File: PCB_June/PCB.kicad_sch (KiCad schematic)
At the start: 26 parts, among them J2 FH34SRJ-24S-0.5SH_99_, J9 61302421121, Q1 BSS138, Q2 S8050, U3 AO3401

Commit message: yur
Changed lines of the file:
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@@
 	(wire
 		(pts
-			(xy 53.34 130.81) (xy 60.96 130.81)
+			(xy 53.34 130.81) (xy 73.66 130.81)
 		)
 		(stroke
@@
 	(wire
 		(pts
-			(xy 53.34 128.27) (xy 60.96 128.27)
+			(xy 53.34 128.27) (xy 73.66 128.27)
 		)
 		(stroke
@@
 	(wire
 		(pts
-			(xy 53.34 123.19) (xy 60.96 123.19)
+			(xy 53.34 123.19) (xy 73.66 123.19)
 		)
 		(stroke
@@
 	(wire
 		(pts
-			(xy 53.34 125.73) (xy 60.96 125.73)
+			(xy 53.34 125.73) (xy 73.66 125.73)
 		)
 		(stroke
@@
 			)
 			(justify left bottom)
+		)
+	)
+	(global_label "EPD_CS"
+		(shape input)
+		(at 73.66 130.81 0)
+		(fields_autoplaced yes)
+		(effects
+			(font
+				(size 1.27 1.27)
+			)
+			(justify left)
+		)
+		(property "Intersheetrefs" "${INTERSHEET_REFS}"
+			(at 83.7813 130.81 0)
+			(effects
+				(font
+					(size 1.27 1.27)
+				)
+				(justify left)
+				(hide yes)
+			)
+		)
+	)
+	(global_label "EPD_BUSY"
+		(shape input)
+		(at 73.66 123.19 0)
+		(fields_autoplaced yes)
+		(effects
+			(font
+				(size 1.27 1.27)
+			)
+			(justify left)
+		)
+		(property "Intersheetrefs" "${INTERSHEET_REFS}"
+			(at 86.2004 123.19 0)
+			(effects
+				(font
+					(size 1.27 1.27)
+				)
+				(justify left)
+				(hide yes)
+			)
 		)
 	)
@@
 			(effects
 				(font
+					(size 1.27 1.27)
+				)
+				(justify left)
+				(hide yes)
+			)
+		)
+	)
+	(global_label "EPD_RST"
+		(shape input)
+		(at 73.66 125.73 0)
+		(fields_autoplaced yes)
+		(effects
+			(font
+				(size 1.27 1.27)
+			)
+			(justify left)
+		)
+		(property "Intersheetrefs" "${INTERSHEET_REFS}"
+			(at 84.7489 125.73 0)
+			(effects
+				(font
+					(size 1.27 1.27)
+				)
+				(justify left)
+				(hide yes)
+			)
+		)
+	)
+	(global_label "EPD_DC"
+		(shape input)
+		(at 73.66 128.27 0)
+		(fields_autoplaced yes)
+		(effects
+			(font
+				(size 1.27 1.27)
+			)
+			(justify left)
+		)
+		(property "Intersheetrefs" "${INTERSHEET_REFS}"
+			(at 83.8418 128.27 0)
+			(effects
+				(font

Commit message: MCB
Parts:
- C17: value 104 -> 0.1u
- L1: value 10u -> 10uH
- R2, R4: value 10K -> 10k
- R3, R5: value 47K -> 47k
- R6: value 100K -> 100k
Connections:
- net EPD_PWR: now also R3.2, R4.2
- no-connect marks 0 -> 11
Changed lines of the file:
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@@
 		(color 0 0 0 0)
 	)
+	(no_connect
+		(at 53.34 110.49)
+	)
+	(no_connect
+		(at 142.24 119.38)
+	)
+	(no_connect
+		(at 142.24 111.76)
+	)
+	(no_connect
+		(at 119.38 114.3)
+	)
+	(no_connect
+		(at 53.34 148.59)
+	)
+	(no_connect
+		(at 53.34 102.87)
+	)
+	(no_connect
+		(at 142.24 134.62)
+	)
+	(no_connect
+		(at 53.34 118.11)
+	)
+	(no_connect
+		(at 53.34 115.57)
+	)
+	(no_connect
+		(at 119.38 129.54)
+	)
+	(no_connect
+		(at 119.38 116.84)
+	)
 	(wire
 		(pts
@@
 	(wire
 		(pts
-			(xy 91.44 48.26) (xy 96.52 48.26)
-		)
-		(stroke
-			(width 0)
-			(type default)
-		)
-	)
-	(wire
-		(pts
 			(xy 107.95 26.67) (xy 107.95 29.21)
 		)
@@
 	(wire
 		(pts
+			(xy 86.36 48.26) (xy 96.52 48.26)
+		)
+		(stroke
+			(width 0)
+			(type default)
+		)
+	)
+	(wire
+		(pts
 			(xy 114.3 26.67) (xy 107.95 26.67)
 		)
@@
 		)
 	)
-	(label "GND"
-		(at 127 60.96 0)
+	(label "3V3_OUT"
+		(at 36.83 41.91 270)
 		(effects
 			(font
 				(size 1.27 1.27)
 			)
-			(justify left bottom)
+			(justify right bottom)
 		)
 	)
-	(label "RESE"
-		(at 149.86 114.3 0)
+	(label "GND"
+		(at 127 60.96 0)
 		(effects
 			(font
@@
 	)
 	(label "RESE"
-		(at 46.99 22.86 0)
-		(effects
-			(font
-				(size 1.27 1.27)
-			)
-			(justify left bottom)
-		)
-	)
-	(label "3V3_OUT"
-		(at 36.83 46.99 90)
+		(at 149.86 114.3 0)
 		(effects
 			(font
@@
 		)
 	)
-	(label "EPD_PWR"
-		(at 86.36 48.26 0)
+	(label "RESE"
+		(at 46.99 22.86 0)
 		(effects
 			(font
@@
 		)
 	)
-	(label "3V3_OUT"
-		(at 36.83 46.99 90)
-		(effects
-			(font
-				(size 1.27 1.27)
-			)
-			(justify left bottom)
-		)
-	)
 	(label "SUB20"
 		(at 60.96 151.13 0)
@@
 		)
 	)
-	(label "3V3_OUT"
-		(at 36.83 46.99 90)
-		(effects
-			(font
-				(size 1.27 1.27)
-			)
-			(justify left bottom)
-		)
-	)
 	(label "EPD_SCK"
 		(at 149.86 127 0)
@@
 		)
 	)
-	(label "EPD_PWR"
-		(at 86.36 48.26 0)
-		(effects
-			(font
-				(size 1.27 1.27)
-			)
-			(justify left bottom)
-		)
-	)
 	(label "GND"
 		(at 149.86 132.08 0)
@@
 		)
 	)
-	(label "EPD_PWR"
-		(at 86.36 48.26 0)
-		(effects
-			(font
-				(size 1.27 1.27)
-			)
-			(justify left bottom)
-		)
-	)
 	(label "VGL"
 		(at 149.86 139.7 0)
@@
 		)
 	)
-	(label "VGL"
-		(at 60.96 158.75 0)
+	(label "EPD_PWR"
+		(at 86.36 48.26 0)
 		(effects
 			(font
@@
 		)
 	)
-	(label "GND"
-		(at 86.36 43.18 90)
+	(label "VGL"
+		(at 60.96 158.75 0)
 		(effects
 			(font
@@
 		)
 	)
-	(label "EPD_SCK"
-		(at 60.96 133.35 0)
+	(label "GND"
+		(at 86.36 43.18 90)
 		(effects
 			(font
@@
 		)
 	)
-	(label "3V3_OUT"
-		(at 36.83 46.99 90)
+	(label "EPD_SCK"
+		(at 60.96 133.35 0)
 		(effects
 			(font
@@
 		)
 	)
-	(label "EPD_BUSY"
-		(at 149.86 121.92 0)
+	(label "3V3_OUT"
+		(at 130.81 20.32 0)
 		(effects
 			(font
@@
 		)
 	)
-	(label "3V3_OUT"
-		(at 130.81 26.67 0)
+	(label "EPD_BUSY"
+		(at 149.86 121.92 0)
 		(effects
 			(font
@@
 		)
 	)
-	(label "EPD_PWR"
-		(at 86.36 48.26 0)
-		(effects
-			(font
-				(size 1.27 1.27)
-			)
-			(justify left bottom)
-		)
-	)
 	(label "VGH"
 		(at 149.86 137.16 0)
@@
 			)
 		)
-		(property "Value" "47K"
+		(property "Value" "47k"
 			(at 110.49 34.2899 0)
 			(effects
@@
 			)
 		)
-		(property "Value" "10K"
+		(property "Value" "10k"
 			(at 104.14 52.07 90)
 			(effects
@@
 			)
 		)
-		(property "Value" "47K"
+		(property "Value" "47k"
 			(at 99.06 40.6399 0)
 			(effects
@@
 			)
 		)
-		(property "Value" "100K"
+		(property "Value" "100k"
 			(at 113.03 57.1499 0)
 			(effects
@@
 			)
 		)
-		(property "Value" "104"
+		(property "Value" "0.1u"
 			(at 90.17 35.5599 0)
 			(effects
@@
 			)
 		)
-		(property "Value" "10K"
+		(property "Value" "10k"
 			(at 29.21 29.21 90)
 			(effects
@@
 			)
 		)
-		(property "Value" "10u"
+		(property "Value" "10uH"
 			(at 43.18 48.26 90)
 			(effects

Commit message: claire can i get inductor footprint haha
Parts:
- removed L1: 10uH, Inductor_SMD:L_0805_2012Metric_Pad1.05x1.20mm_HandSolder, symbol Device:L
- added L1: WE-MXGI_5030, WE-MXGI_5030:WE-MXGI_5030, symbol WE-MXGI_5030:WE-MXGI_5030
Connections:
- net 3V3_OUT: now also L1.1
- net at C8.2, D3.2 (A), Q1.3 (D): now also L1.2
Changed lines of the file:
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@@
 	)
 	(junction
-		(at 110.49 48.26)
+		(at 34.29 50.8)
 		(diameter 0)
 		(color 0 0 0 0)
 	)
 	(junction
-		(at 121.92 60.96)
+		(at 110.49 48.26)
 		(diameter 0)
 		(color 0 0 0 0)
 	)
 	(junction
-		(at 22.86 161.29)
+		(at 52.07 50.8)
 		(diameter 0)
 		(color 0 0 0 0)
 	)
 	(junction
-		(at 96.52 153.67)
+		(at 121.92 60.96)
 		(diameter 0)
 		(color 0 0 0 0)
 	)
 	(junction
-		(at 52.07 50.8)
+		(at 22.86 161.29)
 		(diameter 0)
 		(color 0 0 0 0)
 	)
 	(junction
-		(at 121.92 40.64)
+		(at 96.52 153.67)
 		(diameter 0)
 		(color 0 0 0 0)
 	)
 	(junction
-		(at 36.83 50.8)
+		(at 121.92 40.64)
 		(diameter 0)
 		(color 0 0 0 0)
@@
 	(wire
 		(pts
-			(xy 21.59 50.8) (xy 21.59 64.77)
+			(xy 52.07 50.8) (xy 52.07 64.77)
 		)
 		(stroke
@@
 	(wire
 		(pts
-			(xy 53.34 151.13) (xy 71.12 151.13)
+			(xy 21.59 50.8) (xy 21.59 64.77)
 		)
 		(stroke
@@
 	(wire
 		(pts
-			(xy 53.34 130.81) (xy 73.66 130.81)
+			(xy 53.34 151.13) (xy 71.12 151.13)
 		)
 		(stroke
@@
 	(wire
 		(pts
-			(xy 78.74 158.75) (xy 96.52 158.75)
+			(xy 53.34 130.81) (xy 73.66 130.81)
 		)
 		(stroke
@@
 	(wire
 		(pts
-			(xy 36.83 77.47) (xy 36.83 83.82)
+			(xy 78.74 158.75) (xy 96.52 158.75)
 		)
 		(stroke
@@
 	(wire
 		(pts
-			(xy 107.95 26.67) (xy 107.95 29.21)
+			(xy 36.83 77.47) (xy 36.83 83.82)
 		)
 		(stroke
@@
 	(wire
 		(pts
-			(xy 46.99 50.8) (xy 52.07 50.8)
+			(xy 107.95 26.67) (xy 107.95 29.21)
 		)
 		(stroke
@@
 	(wire
 		(pts
-			(xy 36.83 50.8) (xy 39.37 50.8)
-		)
-		(stroke
-			(width 0)
-			(type default)
-		)
-	)
-	(wire
-		(pts
 			(xy 21.59 43.18) (xy 21.59 50.8)
 		)
@@
 	(wire
 		(pts
-			(xy 33.02 50.8) (xy 36.83 50.8)
+			(xy 33.02 50.8) (xy 34.29 50.8)
 		)
 		(stroke
@@
 	(wire
 		(pts
+			(xy 34.29 50.8) (xy 35.56 50.8)
+		)
+		(stroke
+			(width 0)
+			(type default)
+		)
+	)
+	(wire
+		(pts
 			(xy 111.76 119.38) (xy 119.38 119.38)
 		)
@@
 	(wire
 		(pts
-			(xy 52.07 50.8) (xy 52.07 64.77)
+			(xy 124.46 26.67) (xy 130.81 26.67)
 		)
 		(stroke
@@
 	(wire
 		(pts
-			(xy 124.46 26.67) (xy 130.81 26.67)
+			(xy 33.02 64.77) (xy 36.83 64.77)
 		)
 		(stroke
@@
 	(wire
 		(pts
-			(xy 33.02 64.77) (xy 36.83 64.77)
+			(xy 34.29 41.91) (xy 34.29 50.8)
 		)
 		(stroke
@@
 	(wire
 		(pts
-			(xy 36.83 41.91) (xy 36.83 50.8)
+			(xy 121.92 31.75) (xy 121.92 40.64)
 		)
 		(stroke
@@
 	(wire
 		(pts
-			(xy 121.92 31.75) (xy 121.92 40.64)
+			(xy 52.07 77.47) (xy 52.07 83.82)
 		)
 		(stroke
@@
 	(wire
 		(pts
-			(xy 52.07 77.47) (xy 52.07 83.82)
+			(xy 50.8 50.8) (xy 52.07 50.8)
 		)
 		(stroke
@@
 	)
 	(label "3V3_OUT"
-		(at 36.83 41.91 270)
+		(at 34.29 41.91 270)
 		(effects
 			(font
@@
 	)
 	(symbol
+		(lib_id "WE-MXGI_5030:WE-MXGI_5030")
+		(at 43.18 50.8 0)
+		(unit 1)
+		(exclude_from_sim no)
+		(in_bom yes)
+		(on_board yes)
+		(dnp no)
+		(fields_autoplaced yes)
+		(property "Reference" "L1"
+			(at 42.7355 43.18 0)
+			(effects
+				(font
+					(size 1.27 1.27)
+				)
+			)
+		)
+		(property "Value" "WE-MXGI_5030"
+			(at 42.7355 45.72 0)
+			(effects
+				(font
+					(size 1.27 1.27)
+				)
+			)
+		)
+		(property "Footprint" "WE-MXGI_5030:WE-MXGI_5030"
+			(at 43.18 50.8 0)
+			(effects
+				(font
+					(size 1.27 1.27)
+				)
+				(justify bottom)
+				(hide yes)
+			)
+		)
+		(property "Datasheet" ""
+			(at 43.18 50.8 0)
+			(effects
+				(font
+					(size 1.27 1.27)
+				)
+				(hide yes)
+			)
+		)
+		(property "Description" ""
+			(at 43.18 50.8 0)
+			(effects
+				(font
+					(size 1.27 1.27)
+				)
+				(hide yes)
+			)
+		)
+		(pin "1"
+		)
+		(pin "2"
+		)
+		(instances
+			(project ""
+				(path "/8dcae476-bf02-4dea-8567-670805b7ab7c/9f33d424-8f8c-499b-911f-2b5f72ba0270"
+					(reference "L1")
+					(unit 1)
+				)
+			)
+		)
+	)
+	(symbol
 		(lib_id "Device:C")
 		(at 74.93 161.29 90)
@@
 					(unit 1)
 				)
-			)
-		)
-	)
-	(symbol
-		(lib_id "Device:L")
-		(at 43.18 50.8 90)
-		(unit 1)
-		(exclude_from_sim no)
-		(in_bom yes)
-		(on_board yes)
-		(dnp no)
-		(fields_autoplaced yes)
-		(property "Reference" "L1"
-			(at 43.18 45.72 90)
-			(effects
-				(font
-					(size 1.27 1.27)
-				)
-			)
-		)
-		(property "Value" "10uH"
-			(at 43.18 48.26 90)
-			(effects
-				(font
-					(size 1.27 1.27)
-				)
-			)
-		)
-		(property "Footprint" "Inductor_SMD:L_0805_2012Metric_Pad1.05x1.20mm_HandSolder"
-			(at 43.18 50.8 0)
-			(effects
-				(font
-					(size 1.27 1.27)
-				)
-				(hide yes)
-			)
-		)
-		(property "Datasheet" "~"
-			(at 43.18 50.8 0)
-			(effects
-				(font
-					(size 1.27 1.27)
-				)
-				(hide yes)
-			)
-		)
-		(property "Description" "Inductor"
-			(at 43.18 50.8 0)
-			(effects
-				(font
-					(size 1.27 1.27)
-				)
-				(hide yes)
-			)
-		)
-		(pin "2"
-		)
-		(pin "1"
-		)
-		(instances
-			(project ""
-				(path "/4d36fe0e-b49e-45a2-8e76-66c0323912e5"
-					(reference "L201")
-					(unit 1)
-				)
-			)
-			(project "EE 447"
-				(path "/8dcae476-bf02-4dea-8567-670805b7ab7c/9f33d424-8f8c-499b-911f-2b5f72ba0270"
-					(reference "L1")
-					(unit 1)
-				)

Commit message: footprint
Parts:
- L1: footprint WE-MXGI_5030:WE-MXGI_5030 -> Custom:WE-MXGI_5030
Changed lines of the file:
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@@
 			)
 		)
-		(property "Footprint" "WE-MXGI_5030:WE-MXGI_5030"
+		(property "Footprint" "Custom:WE-MXGI_5030"
 			(at 43.18 50.8 0)
 			(effects

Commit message: added power digikey links
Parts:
- C10, C11, C12, C13, C14, C15, C16, C9: Part Number (none) -> CL21B105KBFNNNE
- C7, C8: Part Number (none) -> GRM21BR61H475KE51L
- R2, R4: Part Number (none) -> RC0805FR-0710KL
- R6: Part Number (none) -> AC0805FR-07100KL
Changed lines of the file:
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@@
 			)
 		)
-		(property "Datasheet" "~"
+		(property "Datasheet" "https://www.digikey.com/en/products/detail/samsung-electro-mechanics/CL21B105KBFNNNE/3886687"
 			(at 74.93 161.29 0)
 			(effects
@@
 			)
 		)
+		(property "Part Number" "CL21B105KBFNNNE"
+			(at 74.93 161.29 0)
+			(effects
+				(font
+					(size 1.27 1.27)
+				)
+				(hide yes)
+			)
+		)
 		(pin "1"
 		)
@@
 			)
 		)
-		(property "Datasheet" "~"
+		(property "Datasheet" "https://www.digikey.com/en/products/detail/samsung-electro-mechanics/CL21B105KBFNNNE/3886687"
 			(at 74.93 138.43 0)
 			(effects
@@
 		)
 		(property "Description" "Unpolarized capacitor"
+			(at 74.93 138.43 0)
+			(effects
+				(font
+					(size 1.27 1.27)
+				)
+				(hide yes)
+			)
+		)
+		(property "Part Number" "CL21B105KBFNNNE"
 			(at 74.93 138.43 0)
 			(effects
@@
 			)
 		)
-		(property "Datasheet" "~"
+		(property "Datasheet" "https://www.digikey.com/en/products/detail/murata-electronics/GRM21BR61H475KE51L/4905540"
 			(at 29.21 50.8 0)
 			(effects
@@
 		)
 		(property "Description" "Unpolarized capacitor"
+			(at 29.21 50.8 0)
+			(effects
+				(font
+					(size 1.27 1.27)
+				)
+				(hide yes)
+			)
+		)
+		(property "Part Number" "GRM21BR61H475KE51L"
 			(at 29.21 50.8 0)
 			(effects
@@
 			)
 		)
-		(property "Datasheet" "~"
+		(property "Datasheet" "https://www.digikey.com/en/products/detail/murata-electronics/GRM21BR61H475KE51L/4905540"
 			(at 44.45 64.77 0)
 			(effects
@@
 			)
 		)
+		(property "Part Number" "GRM21BR61H475KE51L"
+			(at 44.45 64.77 0)
+			(effects
+				(font
+					(size 1.27 1.27)
+				)
+				(hide yes)
+			)
+		)
 		(pin "2"
 		)
@@
 			)
 		)
-		(property "Datasheet" "~"
+		(property "Datasheet" "https://www.digikey.com/en/products/detail/samsung-electro-mechanics/CL21B105KBFNNNE/3886687"
 			(at 74.93 151.13 0)
 			(effects
@@
 		)
 		(property "Description" "Unpolarized capacitor"
+			(at 74.93 151.13 0)
+			(effects
+				(font
+					(size 1.27 1.27)
+				)
+				(hide yes)
+			)
+		)
+		(property "Part Number" "CL21B105KBFNNNE"
 			(at 74.93 151.13 0)
 			(effects
@@
 			)
 		)
-		(property "Datasheet" "~"
+		(property "Datasheet" "https://www.digikey.com/en/products/detail/samsung-electro-mechanics/CL21B105KBFNNNE/3886687"
 			(at 74.93 146.05 0)
 			(effects
@@
 			)
 		)
+		(property "Part Number" "CL21B105KBFNNNE"
+			(at 74.93 146.05 0)
+			(effects
+				(font
+					(size 1.27 1.27)
+				)
+				(hide yes)
+			)
+		)
 		(pin "1"
 		)
@@
 			)
 		)
-		(property "Datasheet" "~"
+		(property "Datasheet" "https://www.digikey.com/en/products/detail/yageo/RC0805FR-0710KL/727535"
 			(at 104.14 48.26 0)
 			(effects
@@
 		)
 		(property "Description" "Resistor"
+			(at 104.14 48.26 0)
+			(effects
+				(font
+					(size 1.27 1.27)
+				)
+				(hide yes)
+			)
+		)
+		(property "Part Number" "RC0805FR-0710KL"
 			(at 104.14 48.26 0)
 			(effects
@@
 			)
 		)
-		(property "Datasheet" "~"
+		(property "Datasheet" "https://www.digikey.com/en/products/detail/samsung-electro-mechanics/CL21B105KBFNNNE/3886687"
 			(at 74.93 156.21 0)
 			(effects
@@
 			)
 		)
+		(property "Part Number" "CL21B105KBFNNNE"
+			(at 74.93 156.21 0)
+			(effects
+				(font
+					(size 1.27 1.27)
+				)
+				(hide yes)
+			)
+		)
 		(pin "1"
 		)
@@
 			)
 		)
-		(property "Datasheet" "~"
+		(property "Datasheet" "https://www.digikey.com/en/products/detail/samsung-electro-mechanics/CL21B105KBFNNNE/3886687"
 			(at 73.66 113.03 0)
 			(effects
@@
 			)
 		)
+		(property "Part Number" "CL21B105KBFNNNE"
+			(at 73.66 113.03 0)
+			(effects
+				(font
+					(size 1.27 1.27)
+				)
+				(hide yes)
+			)
+		)
 		(pin "1"
 		)
@@
 			)
 		)
-		(property "Datasheet" "~"
+		(property "Datasheet" "https://www.digikey.com/en/products/detail/samsung-electro-mechanics/CL21B105KBFNNNE/3886687"
 			(at 74.93 158.75 0)
 			(effects
@@
 		)
 		(property "Description" "Unpolarized capacitor"
+			(at 74.93 158.75 0)
+			(effects
+				(font
+					(size 1.27 1.27)
+				)
+				(hide yes)
+			)
+		)
+		(property "Part Number" "CL21B105KBFNNNE"
 			(at 74.93 158.75 0)
 			(effects
@@
 			)
 		)
-		(property "Datasheet" "~"
+		(property "Datasheet" "https://www.digikey.com/en/products/detail/yageo/ac0805fr-07100kl/5896520"
 			(at 110.49 55.88 0)
 			(effects
@@
 		)
 		(property "Description" "Resistor"
+			(at 110.49 55.88 0)
+			(effects
+				(font
+					(size 1.27 1.27)
+				)
+				(hide yes)
+			)
+		)
+		(property "Part Number" "AC0805FR-07100KL"
 			(at 110.49 55.88 0)
 			(effects
@@
 			)
 		)
-		(property "Datasheet" "~"
+		(property "Datasheet" "https://www.digikey.com/en/products/detail/samsung-electro-mechanics/CL21B105KBFNNNE/3886687"
 			(at 74.93 153.67 0)
 			(effects
@@
 		)
 		(property "Description" "Unpolarized capacitor"
+			(at 74.93 153.67 0)
+			(effects
+				(font
+					(size 1.27 1.27)
+				)
+				(hide yes)
+			)
+		)
+		(property "Part Number" "CL21B105KBFNNNE"
 			(at 74.93 153.67 0)
 			(effects
@@
 			)
 		)
-		(property "Datasheet" "~"
+		(property "Datasheet" "https://www.digikey.com/en/products/detail/yageo/RC0805FR-0710KL/727535"
 			(at 29.21 33.02 0)
 			(effects
@@
 			(at 29.21 33.02 0)
 			(effects
+				(font
+					(size 1.27 1.27)
+				)
+				(hide yes)
+			)
+		)
+		(property "Part Number" "RC0805FR-0710KL"
+			(at 29.21 33.02 0)
+			(effects

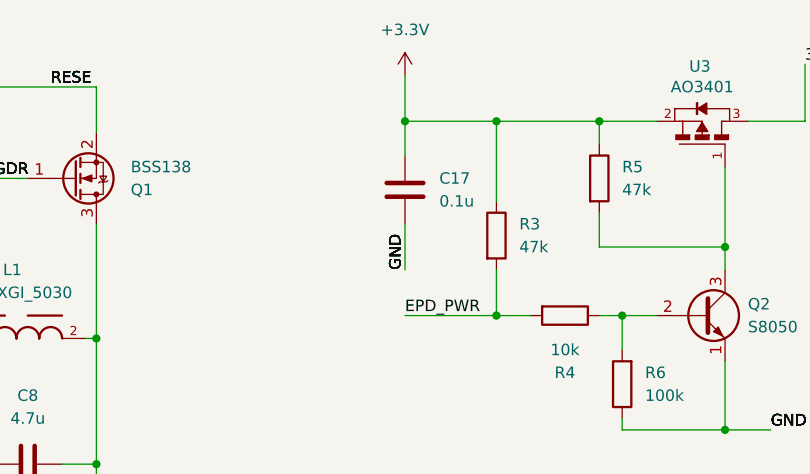
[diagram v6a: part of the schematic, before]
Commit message: finished adding parts and fixing silkscreen
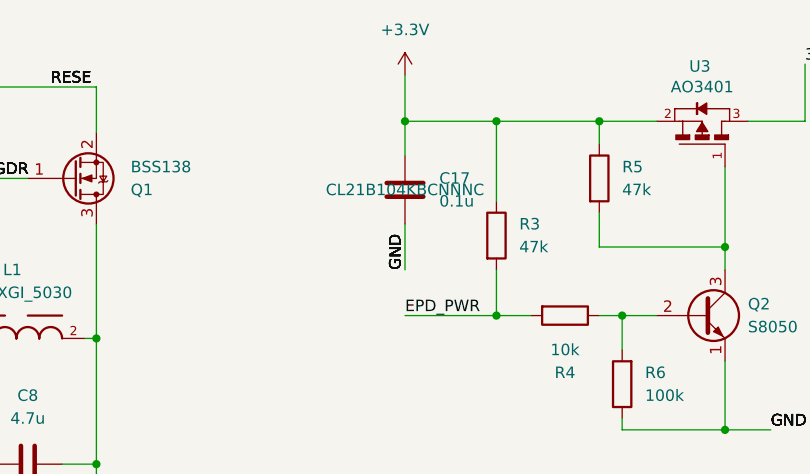
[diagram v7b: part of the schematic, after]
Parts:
- C17: Part Number (none) -> CL21B104KBCNNNC
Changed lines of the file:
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@@
+			)
+		)
+		(property "Part Number" "CL21B104KBCNNNC"
+			(at 86.36 34.29 0)
+			(effects
+				(font
+					(size 1.27 1.27)
+				)
 			)
 		)

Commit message: i try edit stuff but NOT LET ME SYMbOL so i say claire do it hehe ty
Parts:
- R1: value 3 -> 0.47
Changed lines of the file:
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@@
 			)
 		)
-		(property "Value" "3"
+		(property "Value" "0.47"
 			(at 29.21 19.05 90)
 			(effects
@@
 			)
 		)
-		(property "Datasheet" "https://www.hirose.com/en/product/document?clcode=CL0580-1255-6-99&productname=FH34SRJ-24S-0.5SH(99)&series=FH34SRJ&documenttype=2DDrawing&lang=en&documentid=0000990903"
+		(property "Datasheet" "https://www.mouser.com/ProductDetail/Hirose-Connector/FH34SRJ-24S-0.5SH99?qs=vcbW%252B4%252BSTIpKBl5ap9J8Fw%3D%3D"
 			(at 49.53 -33.63 0)
 			(effects
@@
 			)
 		)
-		(property "Datasheet" ""
+		(property "Datasheet" "https://www.digikey.com/en/products/detail/w%C3%BCrth-elektronik/7443845030100/24818486"
 			(at 43.18 50.8 0)
 			(effects
@@
 			)
 		)
-		(property "Datasheet" "https://www.onsemi.com/pub/Collateral/BSS138-D.PDF"
+		(property "Datasheet" "https://www.digikey.com/en/products/detail/onsemi/BSS138/244210"
 			(at 54.61 29.21 0)
 			(effects
